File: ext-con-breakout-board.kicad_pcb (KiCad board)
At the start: 4 copper layers, 46 x 36.6 mm, 9 parts, among them J1 Conn_02x12_Odd_Even, J2 Conn_01x16

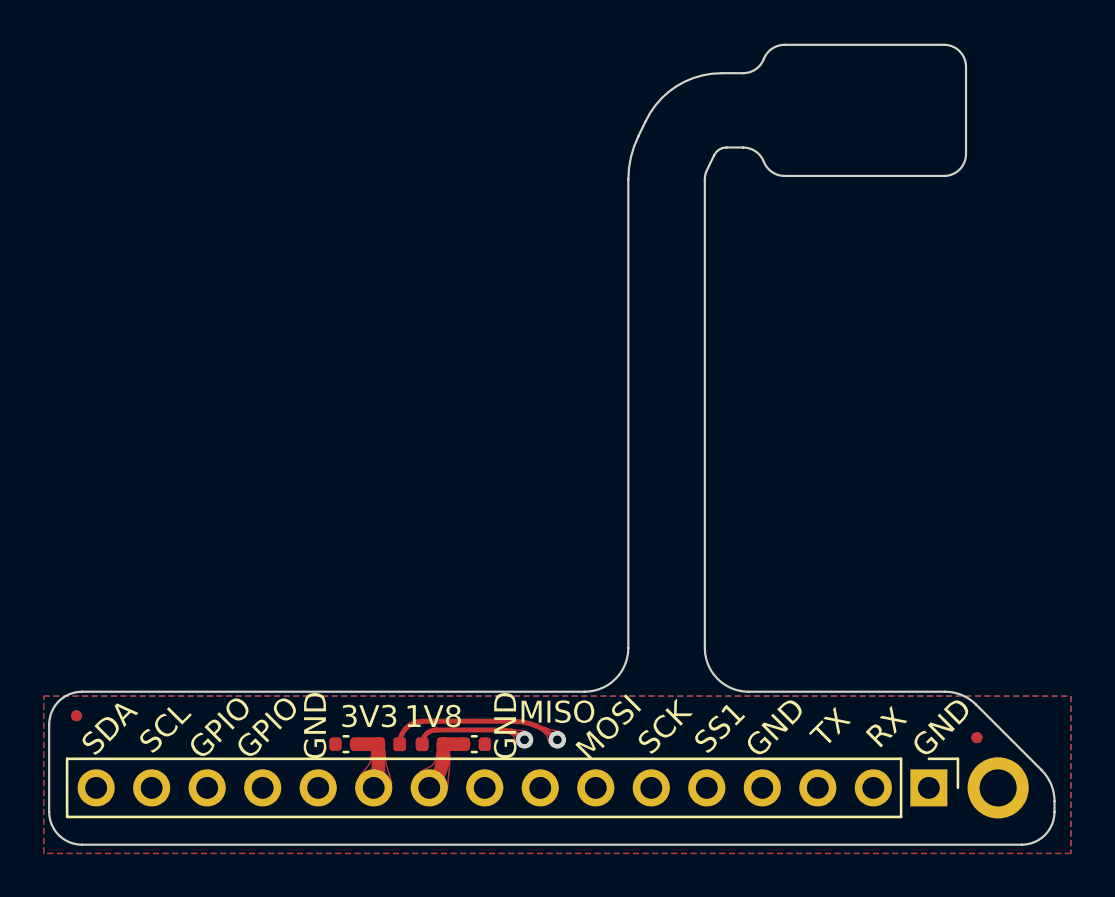
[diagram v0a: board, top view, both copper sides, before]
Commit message: Shrink the flex section by 3.5mm, increment the version to v0.6, re-export the fabrication drawing (PDF), and re-export the gerbers
Also export the schematic as a PDF.
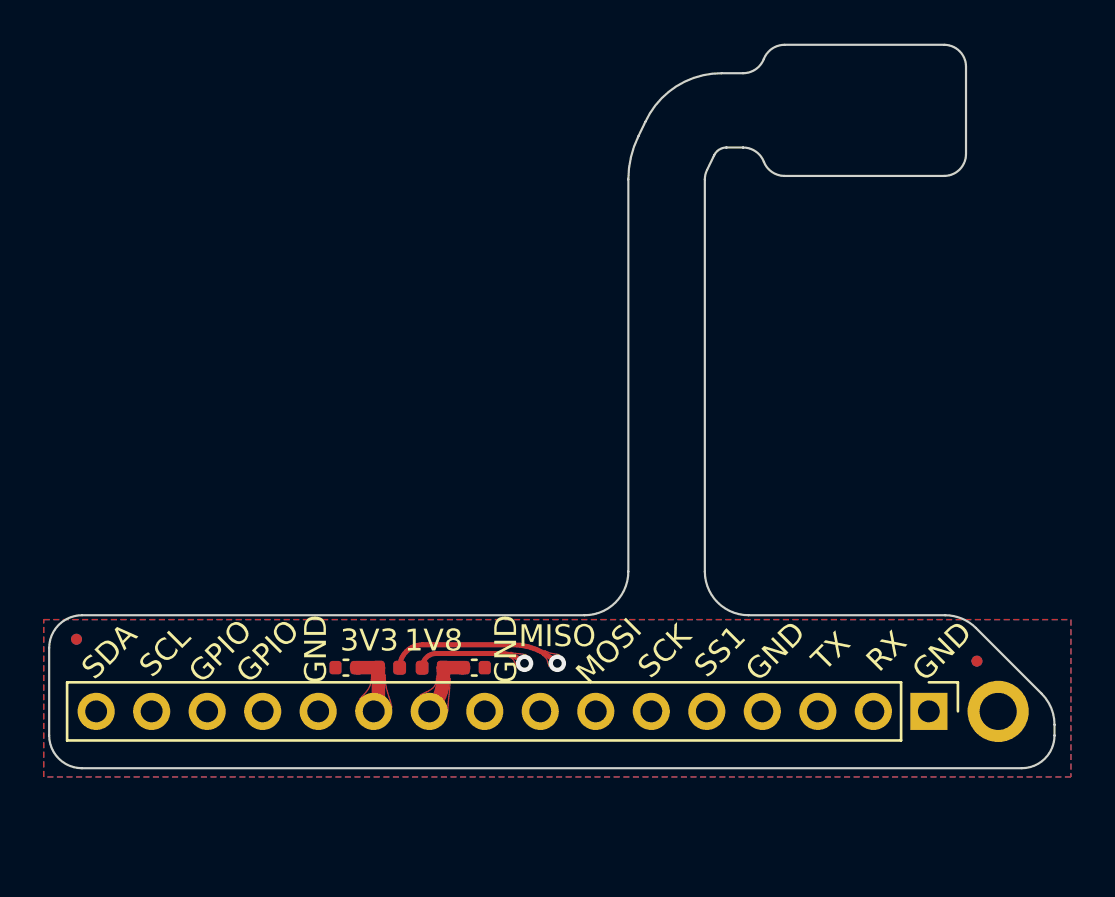
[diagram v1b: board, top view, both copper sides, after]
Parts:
- moved C1 3.50 mm to (109.7, 113.5)
- moved C2 3.50 mm to (103.8, 113.5)
- moved FB1 3.50 mm to (107.8, 113.5)
- moved FB2 3.50 mm to (105.8, 113.5)
- moved FID1 3.50 mm to (91.5, 112.2)
- moved FID2 3.50 mm to (132.7, 113.2)
- moved H1 3.50 mm to (133.7, 115.5)
- moved J2 3.50 mm to (130.5, 115.5)
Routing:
- net /UART1_TXD: track 43.2 -> 39.7 mm
- net /UART1_RXD: track 44.9 -> 41.4 mm
- net /SPI_SS1: track 38.2 -> 34.7 mm
- net /SPI_SCK: track 38.5 -> 35.0 mm
- net /SPI_MOSI: track 39.6 -> 36.1 mm
- net /I2C4_SDA: track 71.0 -> 67.5 mm
- net /I2C4_SCL: track 64.1 -> 60.6 mm
- net /GPIO4_IO28: track 60.6 -> 57.1 mm
- net /GPIO4_IO11: track 56.2 -> 52.7 mm
- net +3V3: track 48.2 -> 44.7 mm
- net +1V8: track 47.7 -> 44.2 mm
- net /SPI_MISO: track 40.7 -> 37.2 mm
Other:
- board size 46 x 36.6 mm -> 46 x 33.1 mm
- board text added: "EXT CON Breakout Board v0.6"
- board text removed: "EXT CON Breakout Board v0.5"
